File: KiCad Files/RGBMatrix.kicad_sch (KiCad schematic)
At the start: 28 parts

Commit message: Update
KiCad files had one small error, fixed it now
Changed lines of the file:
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@@
 (kicad_sch
-	(version 20231120)
+	(version 20250114)
 	(generator "eeschema")
-	(generator_version "8.0")
+	(generator_version "9.0")
 	(paper "A3")
 	(junction

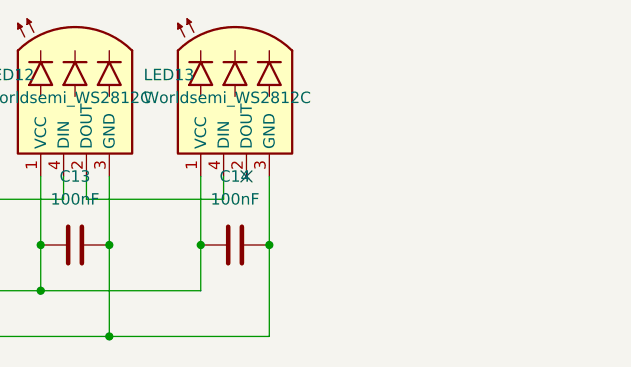
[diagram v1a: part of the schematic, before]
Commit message: Update to revision 1b
- Removed split space
- Updated to 16 5050-leds
- Changed to round routing
- Updated firmware
- Updated production and KiCad-folders to 9.0.1
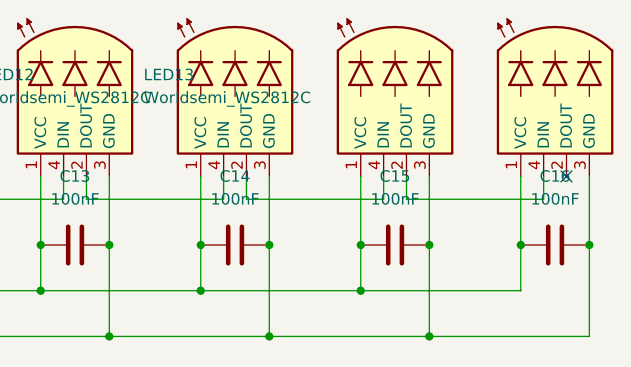
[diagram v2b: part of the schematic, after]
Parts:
- added C15, C16: 100nF, PCM_Capacitor_SMD_Handsoldering_AKL:C_0603_1608Metric_Pad1.08x0.95mm, symbol PCM_Capacitor_US_AKL:C_0603
- added LED15, LED16: Worldsemi_WS2812C, PCM_LED_SMD_AKL:LED_WS2812B_PLCC4_5.0x5.0mm_P3.2mm, symbol PCM_LED_AKL:Worldsemi_WS2812B
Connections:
- net +5V: now also C15.1, C16.1, LED15.1 (VCC), LED16.1 (VCC)
- net GND: now also C15.2, C16.2, LED15.3 (GND), LED16.3 (GND)
- net at LED14.2 (DOUT): now also LED15.4 (DIN)
- new net: LED15.2 (DOUT), LED16.4 (DIN)
